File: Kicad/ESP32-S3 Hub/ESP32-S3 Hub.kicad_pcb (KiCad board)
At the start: 2 copper layers, 60 parts, among them J1 1.27mm 3pin socket, J10 1.27mm 3pin socket, J11 7 pin FPC 0.3mm Panasonic Y3b, J12 1.27mm 3pin socket, J13 TE 3-2363961-0 receptacle, J14 TE 3-2363962-0 Connector, J16 TE 3-2363961-0 receptacle, J17 TE 3-2363962-0 Connector, J2 1.27mm 3pin socket, J21 1.27mm 4 pin socket, J22 1.27mm 4 pin header, J3 7 pin FPC 0.3mm Panasonic Y3b, J4 1.27mm 3pin socket, J5 7 pin FPC 0.3mm Panasonic Y3b, J6 1.27mm 3pin socket, J7 1.27mm 3pin socket, J8 7 pin FPC 0.3mm Panasonic Y3b, J9 1.27mm 3pin socket, SW1 KMR2, SW2 KMR2, SW3 DS04-254-2-04BK-SMT, U1 ESP32-S3, U2 74HC595, U4 SP3485EN, Y1 40mhz, 10ppm, 12pF

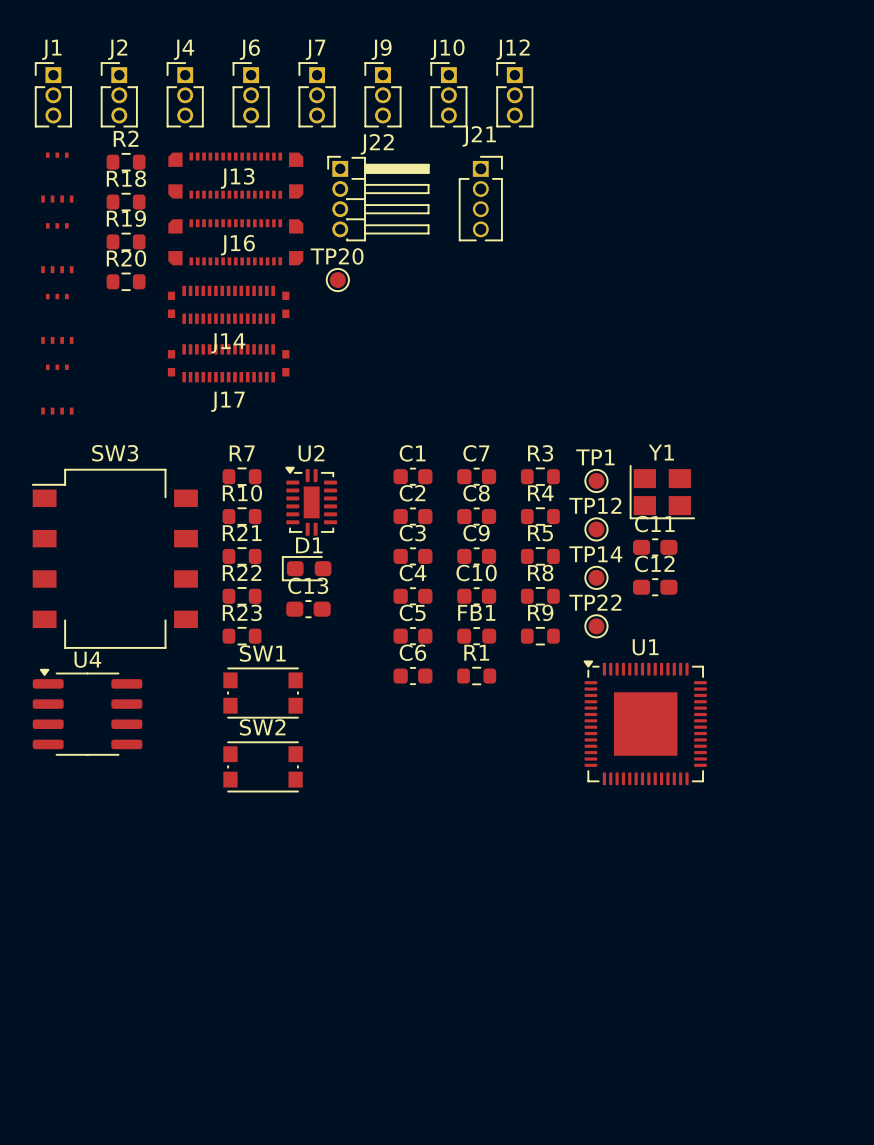
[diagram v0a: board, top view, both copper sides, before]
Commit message: Switching out footprints for smaller variants, dropping rs485 resistors
Space is tight, so I had to downsize the crystal and the reset switches. I also don't have space for the rs485 termination resistors configurable per device, so I have excluded this from the board.
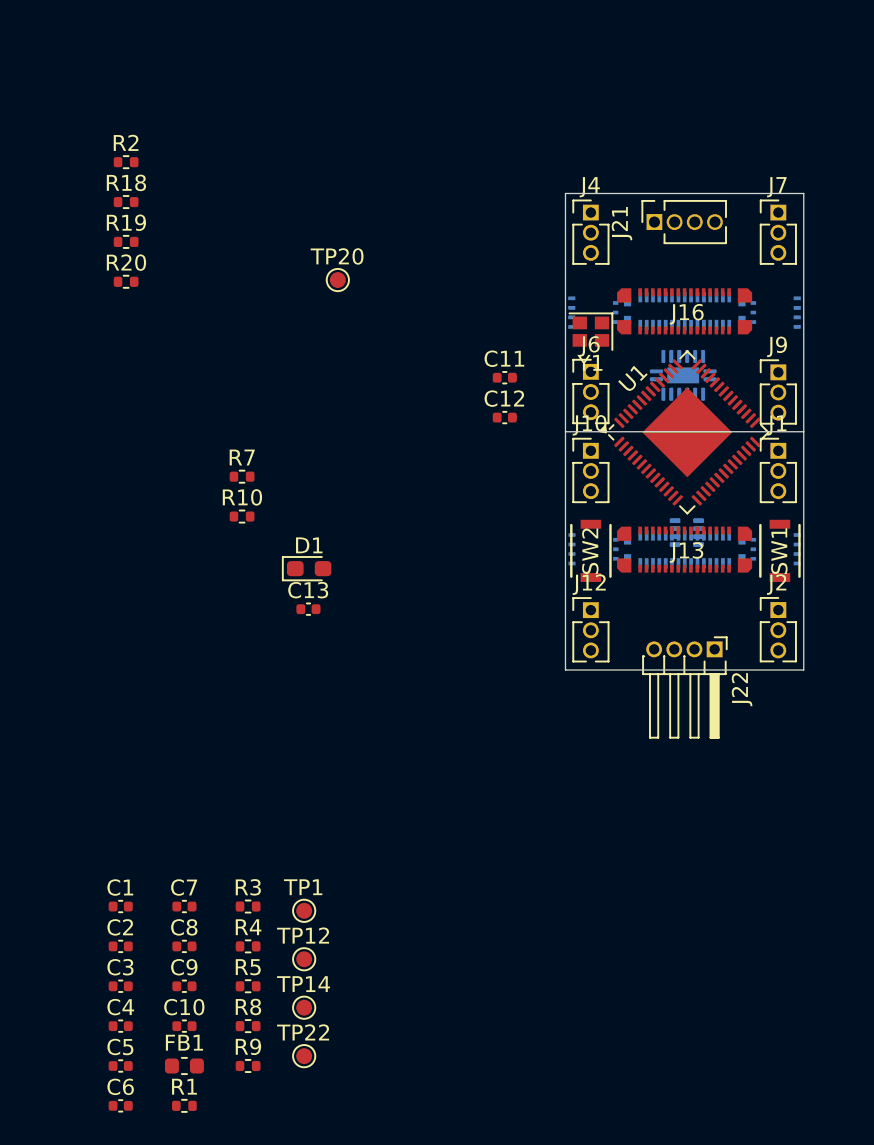
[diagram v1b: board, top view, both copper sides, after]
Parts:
- removed R21, R22, R23: 120 ohm, Resistor_SMD:R_0603_1608Metric
- removed SW3: DS04-254-2-04BK-SMT, Button_Switch_SMD:SW_DIP_SPSTx04_Slide_Omron_A6S-410x_W8.9mm_P2.54mm
- removed U4: SP3485EN, Package_SO:SOIC-8_3.9x4.9mm_P1.27mm
- added U3: THVD1420DRLR, Package_TO_SOT_SMD:SOT-583-8, B.Cu at (155.5, 103.2)
- C1, C10, C2, C3, C4, C5, C6, C7, C8, C9: footprint Capacitor_SMD:C_0603_1608Metric -> Capacitor_SMD:C_0402_1005Metric
- C11, C12: value 16pF -> 12pF; footprint Capacitor_SMD:C_0603_1608Metric_Pad1.08x0.95mm_HandSolder -> Capacitor_SMD:C_0402_1005Metric
- C13: footprint Capacitor_SMD:C_0603_1608Metric_Pad1.08x0.95mm_HandSolder -> Capacitor_SMD:C_0402_1005Metric
- J11, J14, J17, J3, J5, J8, U2: moved to B.Cu
- R1, R10, R18, R19, R2, R20, R3, R4, R5, R7, R8, R9: footprint Resistor_SMD:R_0603_1608Metric -> Resistor_SMD:R_0402_1005Metric
- SW1, SW2: value KMR2 -> Mitsumi R-667996; footprint Button_Switch_SMD:SW_Push_1P1T_NO_CK_KMR2 -> Misumi switches:R-667995_MIT
- Y1: value 40mhz, 10ppm, 12pF -> ABM11-40.000MHZ-B1U-T3, 10ppm, 10pF; footprint Crystal:Crystal_SMD_3225-4Pin_3.2x2.5mm -> Crystal:Crystal_SMD_2016-4Pin_2.0x1.6mm
- moved J2 53.4 mm to (161.3, 108.0)
- moved J1 51.4 mm to (161.3, 98.0)
- moved J3 51.0 mm to (161.2, 104.2), turned to -90 degrees
- moved J8 45.3 mm to (161.2, 89.3), turned to -90 degrees
- moved J5 38.6 mm to (149.6, 104.2), turned to 90 degrees
- moved J22 38.3 mm to (157.3, 110.5), turned to -90 degrees
- moved J13 36.8 mm to (155.4, 104.3)
- moved J11 34.0 mm to (149.6, 89.3), turned to 90 degrees
- moved J12 34.0 mm to (149.5, 108.0)
- moved SW1 33.7 mm to (161.4, 104.3), turned to 90 degrees
- moved TP22 32.7 mm to (131.4, 136.1)
- moved C1 32.7 mm to (119.9, 126.7)
- moved C10 32.7 mm to (123.9, 134.2)
- moved C3 32.7 mm to (119.9, 131.7)
- moved C4 32.7 mm to (119.9, 134.2)
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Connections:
- U2 pad 17: (no net) -> GND
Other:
- board outline added: 15 x 30 mm
- copper layers 2 -> 4

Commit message: Finished basic layout
Everything is crammed in there, I do have some extras bit of space up top for an extra component or two. I probably should take advantage of that space somehow. For routing this thing, I really think i need a 6 or 8 layer board with blind vias.
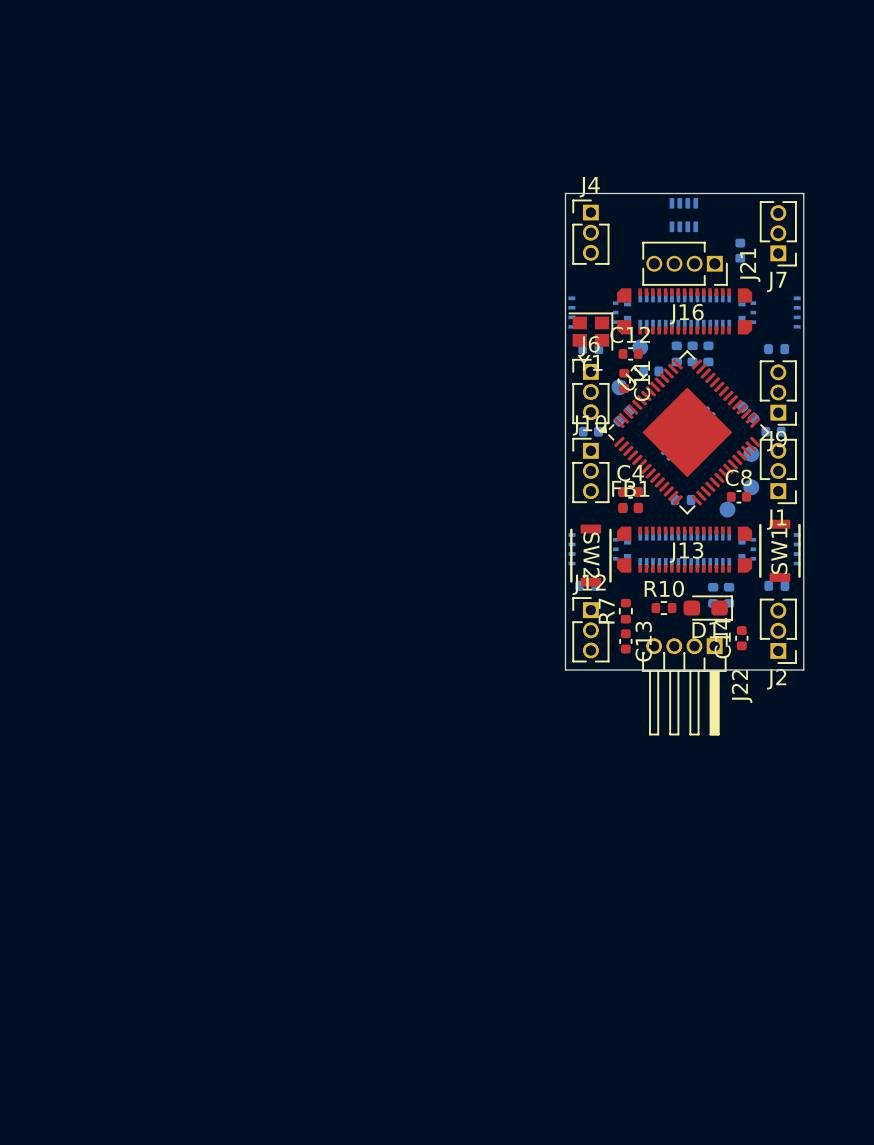
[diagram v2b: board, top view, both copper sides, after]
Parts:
- added C14: 22uF, Capacitor_SMD:C_0402_1005Metric, F.Cu at (159.0, 109.8)
- C1, C10, C2, C3, C5, C6, C7, C9, R1, R18, R19, R2, R20, R3, R4, R5, R8, R9, TP1, TP12, TP14, TP20, TP22: moved to B.Cu
- FB1: value 120ohm imp @100mhz -> 120ohm imp @100mhz, 1 amp; footprint Inductor_SMD:L_0603_1608Metric -> Inductor_SMD:L_0402_1005Metric
- moved C5 57.3 mm to (161.0, 96.8)
- moved C1 56.8 mm to (158.9, 85.4), turned to 90 degrees
- moved C6 53.8 mm to (151.6, 95.8), turned to -135 degrees
- moved C10 50.6 mm to (153.3, 93.0), turned to 180 degrees
- moved R1 49.4 mm to (155.3, 101.1)
- moved R5 49.2 mm to (156.9, 91.9), turned to 90 degrees
- moved R2 48.9 mm to (161.2, 106.5)
- moved C7 47.2 mm to (159.4, 95.6), turned to 135 degrees
- moved R4 46.6 mm to (155.9, 91.9), turned to 90 degrees
- moved TP22 46.6 mm to (151.3, 94.0), turned to 180 degrees
- moved C4 46.5 mm to (152.0, 100.6)
- moved FB1 45.0 mm to (152.0, 101.6)
- moved C8 44.9 mm to (158.8, 100.9)
- moved TP14 44.8 mm to (159.6, 98.2), turned to 180 degrees
- moved R3 44.0 mm to (154.9, 91.9), turned to 90 degrees
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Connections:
- J13 pad 10: MOSI1 -> MISO1
- J13 pad 12: MISO1 -> MOSI1
- J13 pad 19: MISO1 -> MOSI1
- J13 pad 21: MOSI1 -> MISO1
- J14 pad 11: MISO1 -> MOSI1
- J14 pad 20: MISO1 -> MOSI1
- J14 pad 22: MOSI1 -> MISO1
- J14 pad 9: MOSI1 -> MISO1
- J16 pad 10: MOSI1 -> MISO1
- J16 pad 12: MISO1 -> MOSI1
- J16 pad 19: MISO1 -> MOSI1
- J16 pad 21: MOSI1 -> MISO1
- J17 pad 11: MISO1 -> MOSI1
- J17 pad 20: MISO1 -> MOSI1
- J17 pad 22: MOSI1 -> MISO1
- J17 pad 9: MOSI1 -> MISO1
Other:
- outline, holes or cut-outs redrawn
- board text added: "Dividing Line"

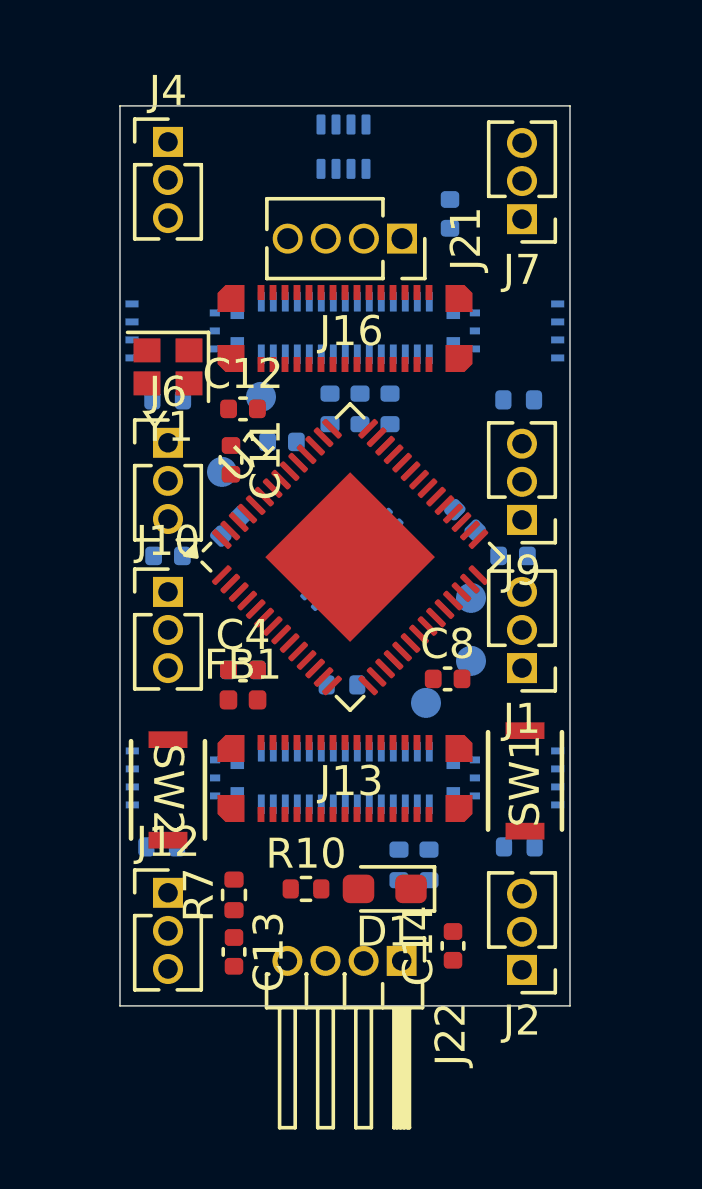
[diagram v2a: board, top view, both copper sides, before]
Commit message: Switched to 6 layer design
I still need to arrange the stackup correctly
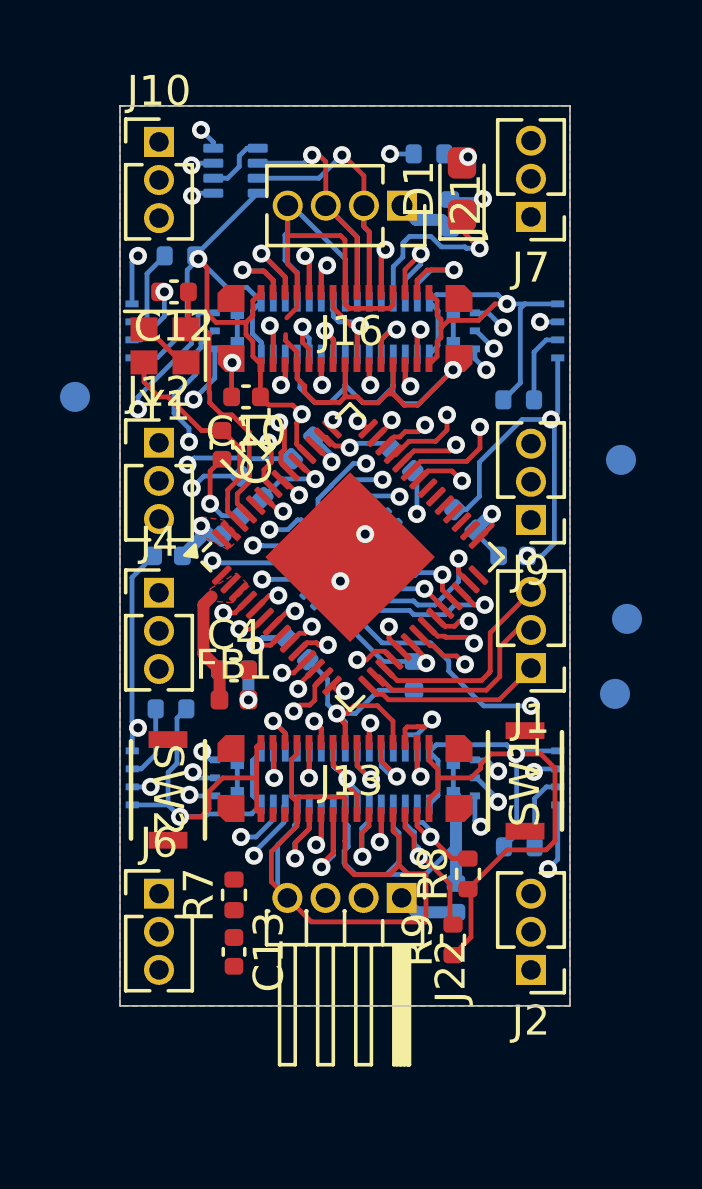
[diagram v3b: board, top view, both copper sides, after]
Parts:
- removed TP22: ~, TestPoint:TestPoint_Pad_D1.0mm
- C10, R8, R9: moved to F.Cu
- C14, C8, R10: moved to B.Cu
- moved R10 24.8 mm to (158.2, 83.4)
- moved D1 23.5 mm to (159.3, 84.6), turned to 90 degrees
- moved J4 15.0 mm to (149.2, 98.0)
- moved J6 15.0 mm to (149.2, 108.1)
- moved J10 15.0 mm to (149.2, 83.0)
- moved J12 15.0 mm to (149.2, 93.0)
- moved TP14 6.79 mm to (164.6, 93.6)
- moved TP1 6.31 mm to (164.4, 101.4)
- moved TP20 6.20 mm to (146.4, 91.5)
- moved TP12 5.39 mm to (164.8, 98.9)
- moved R5 5.28 mm to (152.3, 94.5), turned to 135 degrees
- moved R20 4.82 mm to (149.9, 86.8)
- moved R18 4.61 mm to (149.6, 101.9)
- moved C12 4.53 mm to (149.7, 88.0), turned to 180 degrees
- moved U3 3.69 mm to (151.8, 84.0), turned to 0 degrees
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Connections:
- net RS485_A- renamed RS485-
- net RS485_B+ renamed RS485+
- TP1 pad 1: Net-(U1-GPIO18) -> ShiftRegCLK
- U1 pad 15: SDA1 -> 1A
- U1 pad 16: SCL1 -> 1B
- U1 pad 17: Free1 -> 1C
- U1 pad 18: ShiftRegCLK -> 2A
- U1 pad 19: 1A -> 2B
- U1 pad 21: 1B -> 2C
- U1 pad 22: 1C -> 3A
- U1 pad 23: 2A -> 3B
- U1 pad 24: Net-(U1-GPIO18) -> ShiftRegCLK
- U1 pad 36: 2B -> 3C
- U1 pad 37: 2C -> 4A
- U1 pad 38: 3A -> 4B
- U1 pad 39: 3B -> 4C
- U1 pad 40: 3C -> Free1
- U1 pad 41: 4A -> Free2
- U1 pad 42: 4B -> SDA1
- U1 pad 43: 4C -> SCL1
- U1 pad 52: Net-(U1-GPIO46) -> unconnected-(U1-GPIO46-Pad52)
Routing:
- net VDD: track 0.00 -> 173.8 mm, vias 0 -> 9
- net GND: track 0.00 -> 141.2 mm, vias 0 -> 17
- net RS485-: track 0.00 -> 58.2 mm, vias 0 -> 4
- net RS485+: track 0.00 -> 58.1 mm, vias 0 -> 4
- net MOSI1: track 0.00 -> 44.0 mm, vias 0 -> 9
- net SCL1: track 0.00 -> 41.3 mm, vias 0 -> 5
- net SDA1: track 0.00 -> 36.1 mm, vias 0 -> 5
- net Free1: track 0.00 -> 34.8 mm, vias 0 -> 5
- net MISO1: track 0.00 -> 32.5 mm, vias 0 -> 9
- net CS6: track 0.00 -> 29.8 mm, vias 0 -> 3
- net CS5: track 0.00 -> 22.6 mm, vias 0 -> 3
- net LED: track 0.00 -> 20.6 mm, vias 0 -> 2
- net SCK1: track 0.00 -> 16.7 mm, vias 0 -> 7
- net CS8: track 0.00 -> 16.3 mm, vias 0 -> 3
- net CS7: track 0.00 -> 13.4 mm, vias 0 -> 3
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- added copper zone on B.Cu, net GND
- added copper zone on F.Cu, net GND
- added copper zone on In1.Cu, net GND
- added copper zone on In4.Cu, net GND
- added copper zone on F.Cu, net Net-(C4-Pad1)
- added copper zone on F.Cu, net VDD
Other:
- copper layers 4 -> 6

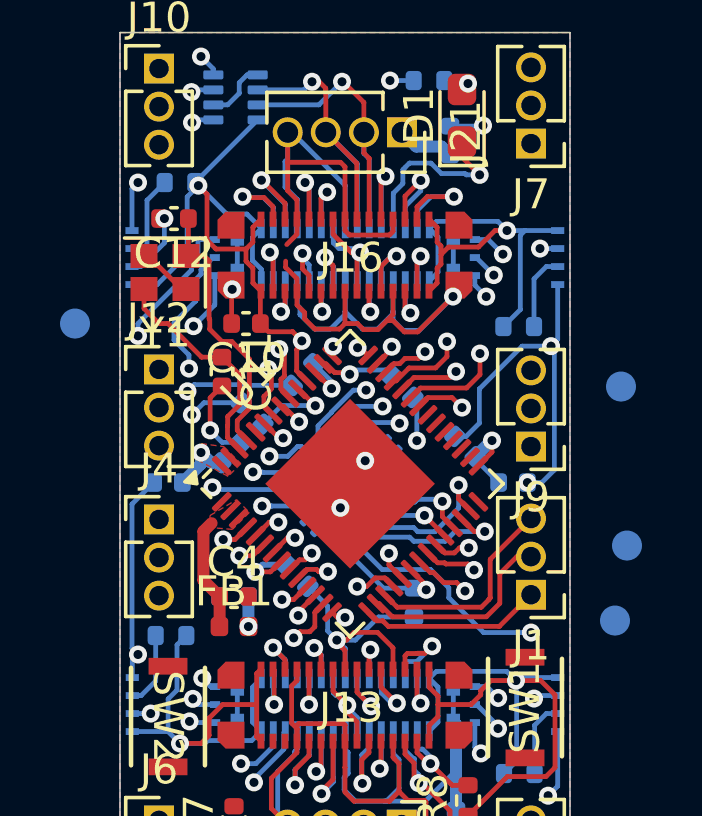
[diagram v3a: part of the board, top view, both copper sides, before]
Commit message: Changed layer stack
I now have a layer stack of Sig/Gnd/Sig/Pwr/Gnd/Sig, which appears to be a common arrangement except I've reversed the order. I added a lot of signals in the middle of the power layer though, because I need more space and I previously had too many signals on my dedicated ground plane.

I also connected Free2 to the correct connectors in the schematic, something I missed when I changed the esp32 pin assignments.
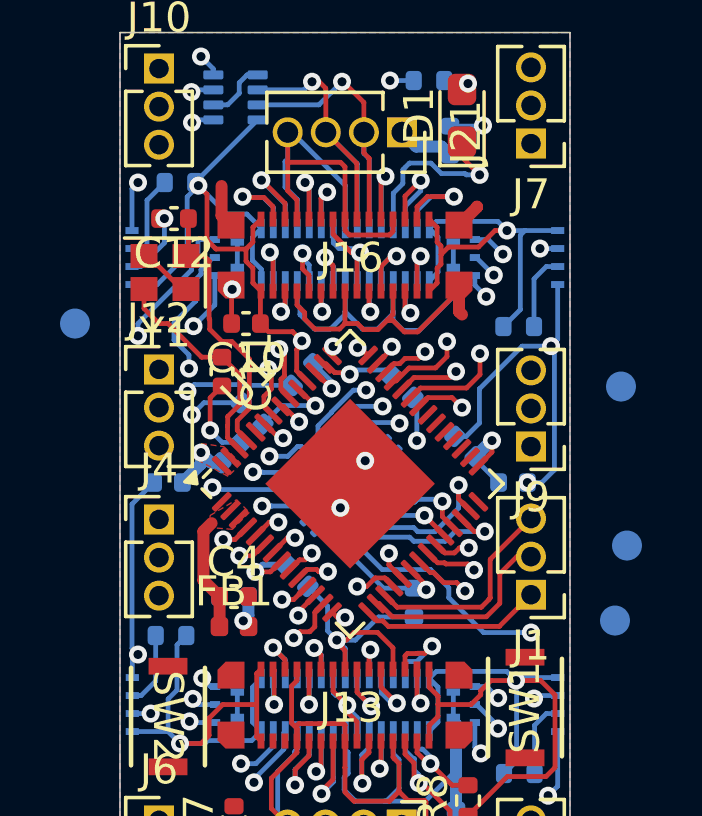
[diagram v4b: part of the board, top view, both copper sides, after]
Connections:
- J13 pad 22: Free1 -> Free2
- J13 pad 9: Free1 -> Free2
- J14 pad 10: Free1 -> Free2
- J14 pad 21: Free1 -> Free2
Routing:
- net Free2: track 0.78 -> 19.5 mm, vias 1 -> 3
- net Free1: track 34.8 -> 16.2 mm, vias 5 -> 3
- net MISO1: track 32.5 -> 38.2 mm
- net VDD: track 173.8 -> 168.2 mm
- net SDA1: track 36.1 -> 34.1 mm
- net SCL1: track 41.3 -> 39.6 mm
- net MOSI1: track 44.0 -> 45.5 mm
- net GND: track 141.2 -> 142.4 mm, vias 17 -> 16
- net RS485+: track 58.1 -> 57.5 mm
- added copper zone on In3.Cu, net VDD
